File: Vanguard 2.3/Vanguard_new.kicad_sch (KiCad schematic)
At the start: 86 parts, among them J1 USB_C_Receptacle_USB2.0_16P, J2 Conn_02x03_Pin, J3 Micro_SD_Card_Det1, J4 STARBOARD_SERVO, J5 PORTSIDE_SERVO, J6 Battery In, J7 EJECTION_SERVO, Q1 BSS138, Q2 BSS138, Q3 BSS138, Q4 BSS138, U1 ATSAMD11D14A-M, U2 ATmega4809-A, U3 AT25DF641A-SH-T, U4 AP2112K-3.3, U5 BD1020HFV, U6 BNO086, U7 TXB0104D, U8 TPS61092, U9 MPM3610AGQV-P, Y1 32.768kHz

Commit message: Force revert commit 97deb62d1ea49336f955e200c1b09f92d203a31d
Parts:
- C12, C13: footprint Capacitor_SMD:C_0201_0603Metric -> (none)
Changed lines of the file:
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@@
 			)
 		)
-		(property "Footprint" "Capacitor_SMD:C_0201_0603Metric"
+		(property "Footprint" ""
 			(at 61.9252 68.58 0)
 			(effects
@@
 			)
 		)
-		(property "Footprint" "Capacitor_SMD:C_0201_0603Metric"
+		(property "Footprint" ""
 			(at 51.7652 68.58 0)
 			(effects

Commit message: bmp370l
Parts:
- added JP1, JP2: Jumper_2_Small_Open, symbol Jumper:Jumper_2_Small_Open
- added R1, R36: 4.7kΩ, symbol Device:R
- added U10: BMP390L, BMP390L:XDCR_BMP390L, symbol BMP390L:BMP390L
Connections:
- net +3.3V: now also R1.1, R36.1, U10.1 (VDDIO), U10.10 (VDD), U10.6 (~{CS})
- net +5V: now also JP2.2 (B)
- net GND: now also JP1.2 (B), U10.3 (VSS/GND), U10.8 (VSS/GND), U10.9 (VSS/GND)
- net SCL: now also R1.2, U10.2 (SCK/SCL)
- net SDA: now also R36.2, U10.4 (SDI/SDO/SDA)
- new net: JP1.1 (A), JP2.1 (A), U10.5 (SDO/DNC/SA0)
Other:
- moved on the sheet: ADR1, C2, C3, C7, R18, R19, R20, R21, R22, R23, R24, TP5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

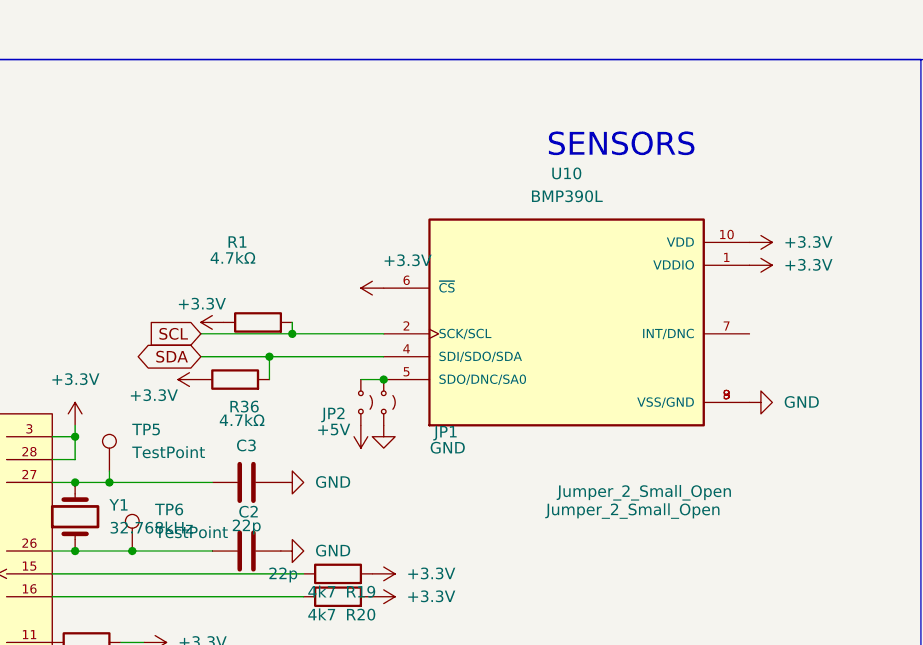
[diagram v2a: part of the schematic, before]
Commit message: i2c adress changes
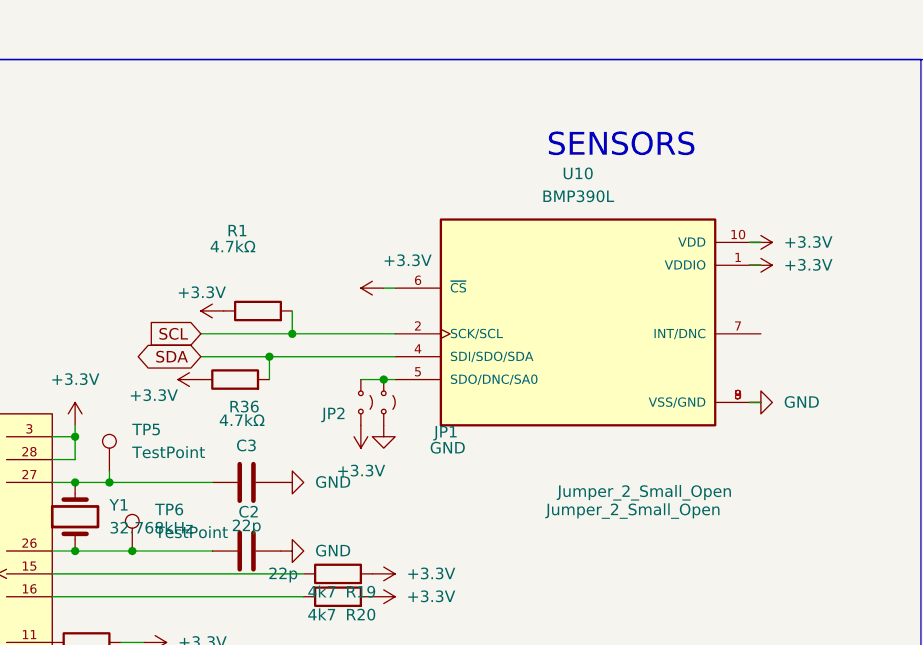
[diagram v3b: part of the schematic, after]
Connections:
- net +3.3V: now also JP2.2 (B)
- net +5V: no longer JP2.2 (B)
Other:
- moved on the sheet: R1, U10
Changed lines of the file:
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@@
 	(wire
 		(pts
+			(xy 171.45 123.19) (xy 170.18 123.19)
+		)
+		(stroke
+			(width 0)
+			(type default)
+		)
+	)
+	(wire
+		(pts
 			(xy 43.18 43.18) (xy 48.26 43.18)
 		)
@@
 	(wire
 		(pts
-			(xy 116.84 133.35) (xy 129.54 133.35)
+			(xy 116.84 133.35) (xy 130.81 133.35)
 		)
 		(stroke
@@
 	(wire
 		(pts
-			(xy 119.38 130.81) (xy 129.54 130.81)
+			(xy 119.38 130.81) (xy 130.81 130.81)
 		)
 		(stroke
@@
 	(wire
 		(pts
+			(xy 171.45 138.43) (xy 170.18 138.43)
+		)
+		(stroke
+			(width 0)
+			(type default)
+		)
+	)
+	(wire
+		(pts
 			(xy 171.45 49.53) (xy 177.8 49.53)
 		)
@@
 	(wire
 		(pts
+			(xy 130.81 135.89) (xy 129.54 135.89)
+		)
+		(stroke
+			(width 0)
+			(type default)
+		)
+	)
+	(wire
+		(pts
 			(xy 288.29 41.91) (xy 288.29 44.45)
 		)
@@
 	(wire
 		(pts
+			(xy 130.81 125.73) (xy 129.54 125.73)
+		)
+		(stroke
+			(width 0)
+			(type default)
+		)
+	)
+	(wire
+		(pts
 			(xy 222.25 58.42) (xy 219.71 58.42)
 		)
@@
 	(wire
 		(pts
-			(xy 119.38 129.54) (xy 119.38 130.81)
+			(xy 119.38 128.27) (xy 119.38 130.81)
 		)
 		(stroke
@@
 	(wire
 		(pts
+			(xy 171.45 120.65) (xy 170.18 120.65)
+		)
+		(stroke
+			(width 0)
+			(type default)
+		)
+	)
+	(wire
+		(pts
 			(xy 58.42 69.85) (xy 58.42 71.12)
 		)
@@
 	(label "RX_UPDI"
 		(at 153.67 50.8 0)
+		(fields_autoplaced yes)
 		(effects
 			(font
@@
 	(label "TX_UPDI"
 		(at 153.67 48.26 0)
+		(fields_autoplaced yes)
 		(effects
 			(font
@@
 	(symbol
 		(lib_id "Device:R")
-		(at 115.57 129.54 90)
+		(at 115.57 128.27 90)
 		(unit 1)
 		(exclude_from_sim no)
@@
 		(dnp no)
 		(property "Reference" "R1"
-			(at 113.284 120.65 90)
+			(at 113.284 119.38 90)
 			(effects
 				(font
@@
 		)
 		(property "Value" "4.7kΩ"
-			(at 112.776 122.428 90)
+			(at 112.776 121.158 90)
 			(effects
 				(font
@@
 		)
 		(property "Footprint" ""
-			(at 115.57 131.318 90)
+			(at 115.57 130.048 90)
 			(effects
 				(font
@@
 		)
 		(property "Datasheet" "~"
-			(at 115.57 129.54 0)
+			(at 115.57 128.27 0)
 			(effects
 				(font
@@
 		)
 		(property "Description" "Resistor"
-			(at 115.57 129.54 0)
+			(at 115.57 128.27 0)
 			(effects
 				(font
@@
 	)
 	(symbol
+		(lib_id "power:+3.3V")
+		(at 127 140.97 180)
+		(unit 1)
+		(exclude_from_sim no)
+		(in_bom yes)
+		(on_board yes)
+		(dnp no)
+		(fields_autoplaced yes)
+		(property "Reference" "#PWR086"
+			(at 127 137.16 0)
+			(effects
+				(font
+					(size 1.27 1.27)
+				)
+				(hide yes)
+			)
+		)
+		(property "Value" "+3.3V"
+			(at 127 146.05 0)
+			(effects
+				(font
+					(size 1.27 1.27)
+				)
+			)
+		)
+		(property "Footprint" ""
+			(at 127 140.97 0)
+			(effects
+				(font
+					(size 1.27 1.27)
+				)
+				(hide yes)
+			)
+		)
+		(property "Datasheet" ""
+			(at 127 140.97 0)
+			(effects
+				(font
+					(size 1.27 1.27)
+				)
+				(hide yes)
+			)
+		)
+		(property "Description" "Power symbol creates a global label with name \"+3.3V\""
+			(at 127 140.97 0)
+			(effects
+				(font
+					(size 1.27 1.27)
+				)
+				(hide yes)
+			)
+		)
+		(pin "1"
+		)
+		(instances
+			(project "Vanguard_new"
+				(path "/972fbf12-2dcd-4fdf-b1c9-8a2880c46640"
+					(reference "#PWR086")
+					(unit 1)
+				)
+			)
+		)
+	)
+	(symbol
 		(lib_id "Device:R")
 		(at 187.96 35.56 0)
@@
 	)
 	(symbol
-		(lib_id "power:+5V")
-		(at 127 140.97 180)
-		(unit 1)
-		(exclude_from_sim no)
-		(in_bom yes)
-		(on_board yes)
-		(dnp no)
-		(property "Reference" "#PWR086"
-			(at 127 137.16 0)
-			(effects
-				(font
-					(size 1.27 1.27)
-				)
-				(hide yes)
-			)
-		)
-		(property "Value" "+5V"
-			(at 123.952 141.478 0)
-			(effects
-				(font
-					(size 1.27 1.27)
-				)
-			)
-		)
-		(property "Footprint" ""
-			(at 127 140.97 0)
-			(effects
-				(font
-					(size 1.27 1.27)
-				)
-				(hide yes)
-			)
-		)
-		(property "Datasheet" ""
-			(at 127 140.97 0)
-			(effects
-				(font
-					(size 1.27 1.27)
-				)
-				(hide yes)
-			)
-		)
-		(property "Description" "Power symbol creates a global label with name \"+5V\""
-			(at 127 140.97 0)
-			(effects
-				(font
-					(size 1.27 1.27)
-				)
-				(hide yes)
-			)
-		)
-		(pin "1"
-		)
-		(instances
-			(project ""
-				(path "/972fbf12-2dcd-4fdf-b1c9-8a2880c46640"
-					(reference "#PWR086")
-					(unit 1)
-				)
-			)
-		)
-	)
-	(symbol
 		(lib_id "power:GND")
 		(at 407.67 162.56 0)
@@
 	(symbol
 		(lib_id "BMP390L:BMP390L")
-		(at 149.86 130.81 0)
+		(at 151.13 130.81 0)
 		(unit 1)
 		(exclude_from_sim no)
@@
 		(fields_autoplaced yes)
 		(property "Reference" "U10"
-			(at 149.86 113.03 0)
+			(at 151.13 113.03 0)
 			(effects
 				(font
@@
 		)
 		(property "Value" "BMP390L"
-			(at 149.86 115.57 0)
+			(at 151.13 115.57 0)
 			(effects
 				(font
@@
 		)
 		(property "Footprint" "BMP390L:XDCR_BMP390L"
-			(at 149.86 130.81 0)
+			(at 151.13 130.81 0)
 			(effects
 				(font
@@
 		)
 		(property "Datasheet" ""
-			(at 149.86 130.81 0)
+			(at 151.13 130.81 0)
 			(effects
 				(font
@@
 		)
 		(property "Description" ""
-			(at 149.86 130.81 0)
+			(at 151.13 130.81 0)
 			(effects
 				(font
@@
 		)
 		(property "MF" "Bosch Sensortec"
-			(at 149.86 130.81 0)
+			(at 151.13 130.81 0)
 			(effects
 				(font
@@
 		)
 		(property "MAXIMUM_PACKAGE_HEIGHT" "0.8 mm"
-			(at 149.86 130.81 0)
+			(at 151.13 130.81 0)
 			(effects
 				(font
@@
 		)
 		(property "Package" "None"
-			(at 149.86 130.81 0)
+			(at 151.13 130.81 0)
 			(effects
 				(font
@@
 		)
 		(property "Price" "None"
-			(at 149.86 130.81 0)
+			(at 151.13 130.81 0)
 			(effects
 				(font
@@
 		)
 		(property "Check_prices" "https://www.snapeda.com/parts/BMP390L/Bosch/view-part/?ref=eda"
-			(at 149.86 130.81 0)
+			(at 151.13 130.81 0)
 			(effects
 				(font
@@
 		)
 		(property "STANDARD" "Manufacturer Recommendation"
-			(at 149.86 130.81 0)
+			(at 151.13 130.81 0)
 			(effects
 				(font
@@
 		)
 		(property "PARTREV" "1.7"
-			(at 149.86 130.81 0)
+			(at 151.13 130.81 0)
 			(effects
 				(font
@@
 		)
 		(property "SnapEDA_Link" "https://www.snapeda.com/parts/BMP390L/Bosch/view-part/?ref=snap"
-			(at 149.86 130.81 0)
+			(at 151.13 130.81 0)
 			(effects
 				(font
@@
 		)
 		(property "MP" "BMP390L"
-			(at 149.86 130.81 0)
+			(at 151.13 130.81 0)
 			(effects
 				(font
@@
 		)
 		(property "Description_1" "\n                        \n                            Pressure Sensor Development Tools Evaluation Shuttle Board for the BMP390L\n                        \n"
-			(at 149.86 130.81 0)
+			(at 151.13 130.81 0)
 			(effects
 				(font
@@
 		)
 		(property "MANUFACTURER" "BOSCH"
-			(at 149.86 130.81 0)
+			(at 151.13 130.81 0)
 			(effects
 				(font
@@
 		)
 		(property "Availability" "In Stock"
-			(at 149.86 130.81 0)
+			(at 151.13 130.81 0)
 			(effects
 				(font
@@
 		)
 		(property "SNAPEDA_PN" "BMP390L"
-			(at 149.86 130.81 0)
+			(at 151.13 130.81 0)
 			(effects
 				(font
@@
 	(symbol
 		(lib_id "power:+3.3V")
-		(at 111.76 129.54 90)
+		(at 111.76 128.27 90)
 		(unit 1)
 		(exclude_from_sim no)
@@
 		(dnp no)
 		(property "Reference" "#PWR084"
-			(at 115.57 129.54 0)
+			(at 115.57 128.27 0)
 			(effects
 				(font
@@
 		)
 		(property "Value" "+3.3V"
-			(at 112.014 127.508 90)
+			(at 112.014 126.238 90)
 			(effects
 				(font
@@
 		)
 		(property "Footprint" ""
-			(at 111.76 129.54 0)
+			(at 111.76 128.27 0)
 			(effects
 				(font
@@
 		)
 		(property "Datasheet" ""
-			(at 111.76 129.54 0)
+			(at 111.76 128.27 0)
 			(effects
 				(font
@@
 		)
 		(property "Description" "Power symbol creates a global label with name \"+3.3V\""
-			(at 111.76 129.54 0)
+			(at 111.76 128.27 0)
 			(effects
 				(font

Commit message: wired mpl370l
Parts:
- C12, C13: footprint (none) -> Capacitor_SMD:C_0201_0603Metric
- JP1, JP2: footprint (none) -> Jumper:SolderJumper-2_P1.3mm_Open_Pad1.0x1.5mm
- R1, R36: footprint (none) -> Resistor_SMD:R_0402_1005Metric
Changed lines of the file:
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@@
 	(label "RX_UPDI"
 		(at 153.67 50.8 0)
-		(fields_autoplaced yes)
 		(effects
 			(font
@@
 	(label "TX_UPDI"
 		(at 153.67 48.26 0)
-		(fields_autoplaced yes)
 		(effects
 			(font
@@
 			)
 		)
-		(property "Footprint" ""
+		(property "Footprint" "Resistor_SMD:R_0402_1005Metric"
 			(at 115.57 130.048 90)
 			(effects
@@
 			)
 		)
-		(property "Footprint" ""
+		(property "Footprint" "Jumper:SolderJumper-2_P1.3mm_Open_Pad1.0x1.5mm"
 			(at 127 138.43 0)
 			(effects
@@
 			)
 		)
-		(property "Footprint" ""
+		(property "Footprint" "Capacitor_SMD:C_0201_0603Metric"
 			(at 61.9252 68.58 0)
 			(effects
@@
 			)
 		)
-		(property "Footprint" ""
+		(property "Footprint" "Jumper:SolderJumper-2_P1.3mm_Open_Pad1.0x1.5mm"
 			(at 129.54 138.43 0)
 			(effects
@@
 			)
 		)
-		(property "Footprint" ""
+		(property "Footprint" "Capacitor_SMD:C_0201_0603Metric"
 			(at 51.7652 68.58 0)
 			(effects
@@
 			)
 		)
-		(property "Footprint" ""
+		(property "Footprint" "Resistor_SMD:R_0402_1005Metric"
 			(at 113.03 137.668 90)
 			(effects

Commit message: pcb; patrick pls check
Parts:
- J1: footprint Connector_USB:USB_C_Receptacle_Amphenol_12401548E4-2A -> Connector_USB:USB_C_Receptacle_GCT_USB4085
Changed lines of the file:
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@@
 			)
 		)
-		(property "Footprint" "Connector_USB:USB_C_Receptacle_Amphenol_12401548E4-2A"
+		(property "Footprint" "Connector_USB:USB_C_Receptacle_GCT_USB4085"
 			(at 31.75 39.37 0)
 			(effects

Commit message: jst ph battery connector inserted- closeout ready for 5ver review
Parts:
- J6: footprint Connector_PinHeader_2.54mm:PinHeader_1x02_P2.54mm_Vertical -> Connector_JST:JST_PH_B2B-PH-K_1x02_P2.00mm_Vertical
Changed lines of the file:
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@@
 	(label "RX_UPDI"
 		(at 153.67 50.8 0)
+		(fields_autoplaced yes)
 		(effects
 			(font
@@
 	(label "TX_UPDI"
 		(at 153.67 48.26 0)
+		(fields_autoplaced yes)
 		(effects
 			(font
@@
 			)
 		)
-		(property "Footprint" "Connector_PinHeader_2.54mm:PinHeader_1x02_P2.54mm_Vertical"
+		(property "Footprint" "Connector_JST:JST_PH_B2B-PH-K_1x02_P2.00mm_Vertical"
 			(at 334.01 163.83 0)
 			(effects

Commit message: footprint
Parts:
- J1: footprint Connector_USB:USB_C_Receptacle_GCT_USB4085 -> Connector_USB:USB-C-SMD_JLC REPLACEMENT
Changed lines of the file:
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@@
 	(label "RX_UPDI"
 		(at 153.67 50.8 0)
-		(fields_autoplaced yes)
 		(effects
 			(font
@@
 	(label "TX_UPDI"
 		(at 153.67 48.26 0)
-		(fields_autoplaced yes)
 		(effects
 			(font
@@
 			)
 		)
-		(property "Footprint" "Connector_USB:USB_C_Receptacle_GCT_USB4085"
+		(property "Footprint" "Connector_USB:USB-C-SMD_JLC REPLACEMENT"
 			(at 31.75 39.37 0)
 			(effects
